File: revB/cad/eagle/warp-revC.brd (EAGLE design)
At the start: 38.1 x 38.1 mm, 145 parts, among them J2 QIIC connector, J3 QIIC connector, J4 DF40FC-20DP-0.4V(51)

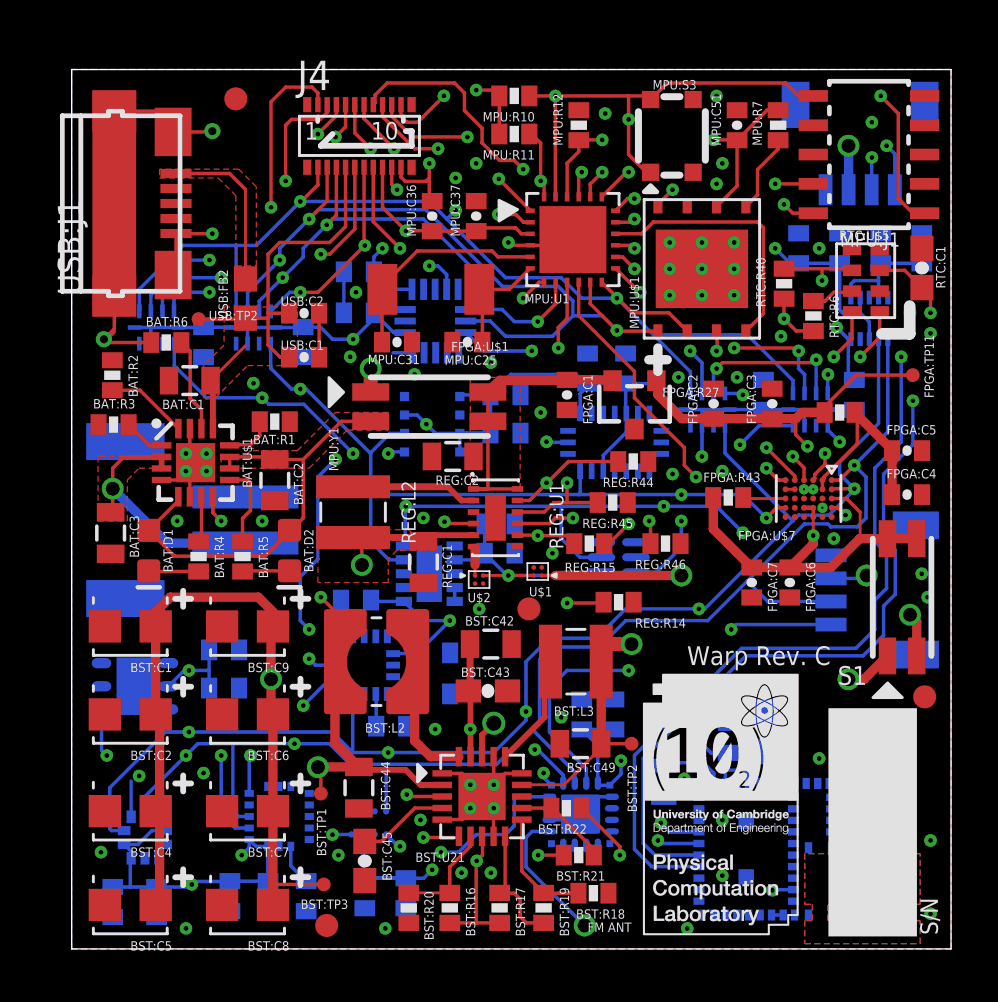
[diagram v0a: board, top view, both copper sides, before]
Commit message: Corrected DRC errors with layout and completed silkscreen
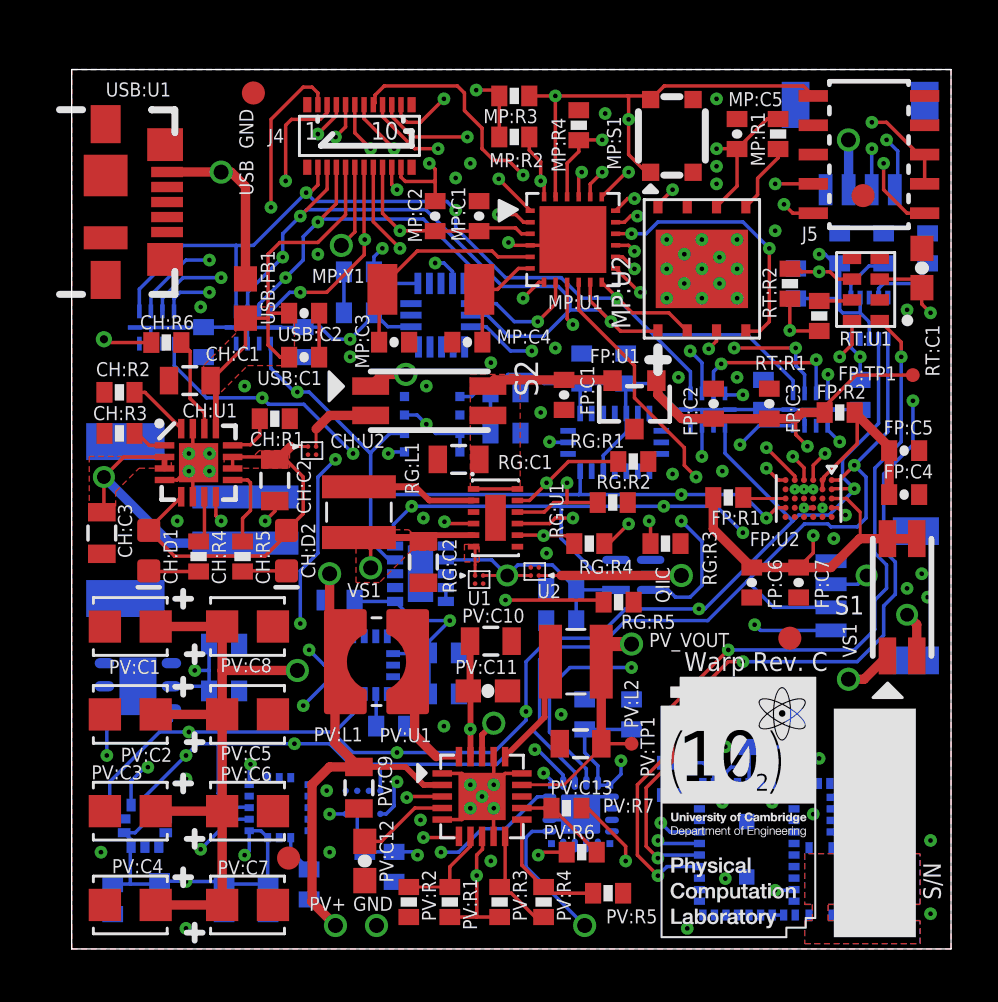
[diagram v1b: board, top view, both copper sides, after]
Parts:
- removed BAT:C3, BST:C42: 4.7uF, SparkFun-Passives:0805
- removed BAT:D2: (no value), SparkFun-LED:LED-0603
- removed BAT:R1: 2.94k, SparkFun-Passives:0402-RES
- removed BAT:R2: 4.32k, SparkFun-Passives:0402-RES
- removed BAT:R3, MPU:R11, MPU:R7, RTC:R40, RTC:R6: 10k, SparkFun-Passives:0402-RES
- removed BAT:U$1: BQ24230VQFN, BQ24230:PVQFN-N16
- removed BST:R16: 4.02M, SparkFun-Passives:0402-RES
- removed BST:R17: 1.3M, SparkFun-Passives:0402-RES
- removed BST:R18: 6.49M, SparkFun-Passives:0402-RES
- removed BST:R19: 5.36M, SparkFun-Passives:0402-RES
- removed BST:R20: 9.09M, SparkFun-Passives:0402-RES
- removed BST:R21: 8.87M, SparkFun-Passives:0402-RES
- removed BST:TP1, BST:TP3, USB:TP2: TPSTP06R, testpad:TP06R
- removed BT:C32, DP:C52, FPGA:C3, FPGA:C4, FPGA:C6, MPU:C37, MPU:C51, SEN1:C28, SEN2:C16, SEN2:C18, SEN2:C20, SEN2:C21, SEN2:C23, SEN2:C34, SEN2:C46, SEN2:C48: 0.1uF, SparkFun-Passives:0402-CAP
- removed DP:U20: ISL23415UTQFN, ISL23415:ISL23415
- removed FD5: FIDUCIAL1X2, SparkFun-Aesthetics:FIDUCIAL-1X2
- removed FPGA:C1, SEN1:C13, SEN1:C27, SEN1:C29, SEN2:C17, SEN2:C22, SEN2:C39, SEN2:C47: 1uF, SparkFun-Passives:0402-CAP
- removed FPGA:C5, SEN2:C15: 10uF, SparkFun-Passives:0402-CAP
- removed MPU:C31: 33pF, SparkFun-Passives:0402-CAP
- removed MPU:C36: 4.7uF (pol), SparkFun-Passives:0402-CAP
- removed REG:C2: 10uF, SparkFun-Passives:0805
- removed REG:L2: 2.2uH, EMCComponents (rev19c):WE-TPC_2828_OLD
- removed RTC:U$5: RV-8803-C7_RTC, Micro Crystal RTC:RV-C7
- removed S3: CHS-02_SWITCH, CHS_SWITCH:CHS-02_SWITCH
- removed SEN1:C50, SEN2:C19: 4.7uF, SparkFun-Passives:0402-CAP
- removed SEN1:U1: ADXL362, ADXL362:ADXL362
- removed SEN1:U10: TCS34725FN, TCS3772:TCS3772
- removed SEN1:U5: CCS811, SparkFun-Sensors:LGA10
- removed SEN2:C24: 10nF (25V), SparkFun-Passives:0402-CAP
- removed SEN2:C35: 22nF, SparkFun-Passives:0402-CAP
- removed SEN2:U16: LPS25H, LPS25H:LPS25H
- removed SEN2:U4: HDC1000, HDC1000:HDC1000
- removed SEN2:U5: L3GD20H, L3GD20H:L3GD20H
- removed SEN2:U9: SI7021, SI7021:SI7021
- removed U$1: MAX40200, MAX40200:DSBGA
- removed USB:J1: J_USB_MICROAB_HIROSE_ZX62-AB-5PA, j_usb_hirose_zx62-ab-5pa:J_USB_MICROAB_HIROSE_ZX62-AB-5PA
- added BT:C2, FP:C1, SA:C4, SA:C7, SA:C9, SB:C10, SB:C18, SB:C2, SB:C8: 1uF, SparkFun-Passives:0402-CAP
- added CH:C3, PV:C10: 4.7uF, SparkFun-Passives:0805
- added CH:D2: (no value), SparkFun-LED:LED-0603
- added CH:R1: 2.94k, SparkFun-Passives:0402-RES
- added CH:R2: 4.32k, SparkFun-Passives:0402-RES
- added CH:R3, MP:R1, MP:R2, RT:R1, RT:R2: 10k, SparkFun-Passives:0402-RES
- added CH:U1: BQ24230VQFN, BQ24230:PVQFN-N16
- added CH:U2, U2: MAX40200, MAX40200:DSBGA
- added DP:C4, FP:C3, FP:C4, FP:C7, MP:C1, MP:C5, SA:C8, SB:C1, SB:C11, SB:C12, SB:C13, SB:C16, SB:C17, SB:C4, SB:C7: 0.1uF, SparkFun-Passives:0402-CAP
- added DP:U4: ISL23415UTQFN, ISL23415:ISL23415
- added FD4: FIDUCIAL1X2, SparkFun-Aesthetics:FIDUCIAL-1X2
- added FP:C5, SB:C5: 10uF, SparkFun-Passives:0402-CAP
- added MP:C2: 4.7uF (pol), SparkFun-Passives:0402-CAP
- added MP:C3: 33pF, SparkFun-Passives:0402-CAP
- added PV:R1: 4.02M, SparkFun-Passives:0402-RES
- added PV:R2: 9.09M, SparkFun-Passives:0402-RES
- added PV:R3: 1.3M, SparkFun-Passives:0402-RES
- added PV:R4: 5.36M, SparkFun-Passives:0402-RES
- added PV:R5: 6.49M, SparkFun-Passives:0402-RES
- added PV:R6: 8.87M, SparkFun-Passives:0402-RES
- added RG:C1: 10uF, SparkFun-Passives:0805
- added RG:L1: 2.2uH, EMCComponents (rev19c):WE-TPC_2828_OLD
- added RT:U1: RV-8803-C7_RTC, Micro Crystal RTC:RV-C7
- added S2: CHS-02_SWITCH, CHS_SWITCH:CHS-02_SWITCH
- added SA:C5, SB:C14: 4.7uF, SparkFun-Passives:0402-CAP
- added SA:U1: ADXL362, ADXL362:ADXL362
- added SA:U3: CCS811, SparkFun-Sensors:LGA10
- added SA:U5: TCS34725FN, TCS3772:TCS3772
- added SB:C15: 22nF, SparkFun-Passives:0402-CAP
- added SB:C6: 10nF (25V), SparkFun-Passives:0402-CAP
- added SB:U2: L3GD20H, L3GD20H:L3GD20H
- added SB:U3: SI7021, SI7021:SI7021
- added SB:U5: LPS25H, LPS25H:LPS25H
- added SB:U7: HDC1000, HDC1000:HDC1000
- added USB:U1: MOLEX_USB_47346-0001MICRO_USB_B, MOLEX MICRO USB:USB-B-MICRO-SMD
- BT:C1: value 1uF -> 0.1uF; device SparkFun-Passives:0603-CAP -> SparkFun-Passives:0402-CAP
- BT:U1: value BGX13S -> BGX13S22GA-V21R
- MP:U2: value AT45DB641E -> AT45DB641E-MHN-Y
- moved FD1 33.0 mm to (9.40, 3.94)
- moved DP:C1 24.4 mm to (5.71, 26.3), turned to 270 degrees
- moved DP:U1 24.1 mm to (3.68, 26.9)
- moved FD2 23.0 mm to (34.3, 32.6)
- moved J2 17.6 mm to (32.9, 15.3), turned to 270 degrees
- moved J3 17.4 mm to (34.2, 32.9), turned to 180 degrees
- moved FD3 6.37 mm to (31.1, 13.5)
- moved DP:U2 4.44 mm to (27.6, 23.4)
- moved DP:C2 3.94 mm to (30.0, 24.0)
- moved BT:C1 0.76 mm to (29.3, 9.40)
- moved BT:Y1 0.28 mm to (25.9, 7.37)
- turned PV:C5 to 0 degrees
- turned PV:C6 to 0 degrees
- turned PV:C7 to 0 degrees
- turned PV:C8 to 0 degrees
- renumbered BAT:C1 to CH:C1, BAT:C2 to CH:C2, BAT:D1 to CH:D1, BAT:R4 to CH:R4, BAT:R5 to CH:R5, BAT:R6 to CH:R6, BST:C1 to PV:C1, BST:C2 to PV:C2, BST:C4 to PV:C3, BST:C43 to PV:C11, BST:C44 to PV:C9, BST:C45 to PV:C12, BST:C49 to PV:C13, BST:C5 to PV:C4, BST:C6 to PV:C5, BST:C7 to PV:C6, BST:C8 to PV:C7, BST:C9 to PV:C8, BST:L2 to PV:L1, BST:L3 to PV:L2, BST:R22 to PV:R7, BST:TP2 to PV:TP1, BST:U21 to PV:U1, DP:C53 to DP:C3, DP:U23 to DP:U3, FPGA:C2 to FP:C2, FPGA:C7 to FP:C6, FPGA:R27 to FP:R2, FPGA:R43 to FP:R1, FPGA:TP11 to FP:TP1, FPGA:U$1 to FP:U1, FPGA:U$7 to FP:U2, MPU:C25 to MP:C4, MPU:J1 to J5, MPU:R10 to MP:R3, MPU:R12 to MP:R4, MPU:S3 to MP:S1, MPU:U$1 to MP:U2, MPU:U1 to MP:U1, MPU:Y1 to MP:Y1, REG:C1 to RG:C2, REG:R14 to RG:R5, REG:R15 to RG:R4, REG:R44 to RG:R1, REG:R45 to RG:R2, REG:R46 to RG:R3, REG:U1 to RG:U1, RTC:C1 to RT:C1, SEN1:C10 to SA:C1, SEN1:C11 to SA:C2, SEN1:C12 to SA:C3, SEN1:C26 to SA:C6, SEN1:U2 to SA:U4, SEN1:U3 to SA:U2, SEN2:C14 to SB:C3, SEN2:C38 to SB:C9, SEN2:U13 to SB:U6, SEN2:U7 to SB:U4, SEN2:U8 to SB:U1, U$2 to U1, USB:FB2 to USB:FB1
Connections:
- net BAT:N$6 renamed CH:N$6
- net BST:LBOOST renamed PV:LBOOST
- net BST:LBUCK renamed PV:LBUCK
- net BST:VREF_SAMP renamed PV:VREF_SAMP
- net FPGA:CRESET_B renamed FP:CRESET_B
- net MPU:AT45DB321F_SPI_CS renamed MP:AT45DB321F_SPI_CS
- net MPU:XTAL0 renamed MP:XTAL0
- net SEN2:N$1 renamed SB:N$1
- net SEN2:SI4705_FMI renamed SB:SI4705_FMI
- removed net BAT:N$1: BAT:R2.2, BAT:U$1.16
- removed net BAT:N$2: BAT:R1.2, BAT:U$1.12
- removed net BAT:N$3: BAT:U$1.7, CH:R4.1
- removed net BAT:N$4: BAT:R3.2, BAT:U$1.1
- removed net BAT:N$5: BAT:U$1.9, CH:R5.1
- removed net BAT:N$7: BAT:D2.C, CH:R5.2
- removed net BAT:N$8: BAT:U$1.14, CH:R6.2
- removed net BOOST_VOUT: PV:C13.1, PV:L2.2, PV:TP1.TP, PV:U1.14, S3.1
- removed net BST:OK_HYST: BST:R17.1, BST:R19.2, PV:U1.10
- removed net BST:OK_PROG: BST:R18.2, BST:R19.1, PV:U1.11
- removed net BST:VBAT_OV: BST:R16.1, BST:R20.2, PV:U1.7
- removed net BST:VOUT_SET: BST:R21.1, PV:R7.2, PV:U1.12
- removed net BST:VRDIV: BST:R16.2, BST:R17.2, BST:R21.2, PV:U1.8
- removed net BST:VSTOR: BST:C42.1, PV:C11.1, PV:U1.19, PV:U1.3, PV:U1.6
- removed net FPGA:ICE40_VCC_PLL: FP:R2.1, FP:U2.B1, FP:U2.B2, FPGA:C4.1, FPGA:C5.1
- removed net FPGA:VCC_1V2: FP:C2.1, FP:R2.2, FP:TP1.TP, FP:U1.1, FP:U2.C2, FPGA:C3.1
- removed net MPU:EXTAL0: MP:U1.P$5, MP:Y1.P$1, MPU:C31.1
- removed net MPU:N$4: MP:U2.5, MPU:R7.1
- removed net PV_VS: BST:TP1.TP, J4.P$15, PV:C9.1, PV:L1.1, PV:U1.2
- removed net REG:SW: REG:L2.1, RG:U1.2
- removed net RTC:N$3: RTC:R6.1, RTC:U$5.7
- removed net SEN1:N$7: SEN1:U5.4, SEN1:U5.5
- removed net SEN2:CAP: SEN2:C24.1, SEN2:U5.P$14
- removed net SEN2:N$17: SB:U4.P$1, SB:U4.P$4, SEN2:C20.1, SEN2:C21.1
- removed net USB:DM: USB:J1.P$2
- removed net USB:DP: USB:J1.P$3
- new net CH:BQ24230_OUT: CH:C2.1, CH:D1.A, CH:D2.A, CH:U1.10, CH:U1.11, CH:U1.5, CH:U2.A1
- new net CH:N$1: CH:R2.2, CH:U1.16
- new net CH:N$2: CH:R1.2, CH:U1.12
- new net CH:N$3: CH:R4.1, CH:U1.7
- new net CH:N$4: CH:R3.2, CH:U1.1
- new net CH:N$5: CH:R5.1, CH:U1.9
- new net CH:N$7: CH:D2.C, CH:R5.2
- new net CH:N$8: CH:R6.2, CH:U1.14
- new net FP:ICE40_VCC_PLL: FP:C4.1, FP:C5.1, FP:R2.1, FP:U2.B1, FP:U2.B2
- new net FP:VCC_1V2: FP:C2.1, FP:C3.1, FP:R2.2, FP:TP1.TP, FP:U1.1, FP:U2.C2
- new net MP:EXTAL0: MP:C3.1, MP:U1.P$5, MP:Y1.P$1
- new net MP:N$4: MP:R1.1, MP:U2.5
- new net PV:OK_HYST: PV:R3.1, PV:R4.2, PV:U1.10
- new net PV:OK_PROG: PV:R4.1, PV:R5.2, PV:U1.11
- new net PV:VBAT_OV: PV:R1.1, PV:R2.2, PV:U1.7
- new net PV:VOUT_SET: PV:R6.1, PV:R7.2, PV:U1.12
- new net PV:VRDIV: PV:R1.2, PV:R3.2, PV:R6.2, PV:U1.8
- new net PV:VSTOR: PV:C10.1, PV:C11.1, PV:U1.19, PV:U1.3, PV:U1.6
- new net PV_VIN: J4.P$15, PV:C9.1, PV:L1.1, PV:U1.2
- new net PV_VOUT: PV:C13.1, PV:L2.2, PV:TP1.TP, PV:U1.14, S2.1
- new net RG:SW: RG:L1.1, RG:U1.2
- new net RT:N$3: RT:R1.1, RT:U1.7
- new net SA:N$7: SA:U3.4, SA:U3.5
- new net SB:CAP: SB:C6.1, SB:U2.P$14
- new net SB:N$17: SB:C12.1, SB:U4.P$1
- new net SB:N$2: SB:C11.1, SB:U4.P$4
- net ADXL362_SPI_CS: now also SA:U1.P$8; no longer SEN1:U1.P$8
- net BAT: now also CH:C3.1, CH:U1.2, CH:U1.3; no longer BAT:C3.1, BAT:U$1.2, BAT:U$1.3
- net BOOST_VBAT: no longer BST:TP3.TP
- net CHARGE_VOUT: now also CH:U2.A2, S2.2; no longer BAT:D2.A, BAT:U$1.10, BAT:U$1.11, BAT:U$1.5, CH:C2.1, CH:D1.A, S3.2
- net FPGA_VS: now also FP:C7.1; no longer FP:U2.C5, FPGA:C6.1
- net GND: now also BT:C2.2, CH:C3.2, CH:R1.1, CH:R2.1, CH:R3.1, CH:U1.15, CH:U1.4, CH:U1.6, CH:U1.8, CH:U1.EP, CH:U2.B2, DP:C4.2, DP:U4.9, FP:C1.2, FP:C3.2, FP:C4.2, FP:C5.2, FP:C7.2, MP:C1.2, MP:C2.2, MP:C3.2, MP:C5.2, PV:C10.2, PV:R2.1, PV:R5.1, RG:C1.2, RT:U1.4, RT:U1.5, SA:C4.2, SA:C5.2, SA:C7.2, SA:C8.2, SA:C9.2, SA:U1.P$12, SA:U1.P$13, SA:U1.P$16, SA:U3.1, SA:U3.7, SA:U3.EP, SA:U5.P$3, SB:C1.2, SB:C10.2, SB:C11.2, SB:C12.2, SB:C13.2, SB:C14.2, SB:C15.2, SB:C16.2, SB:C17.2, SB:C18.2, SB:C2.2, SB:C4.2, SB:C5.2, SB:C6.2, SB:C7.2, SB:C8.2, SB:U2.P$10, SB:U2.P$11, SB:U2.P$12, SB:U2.P$13, SB:U2.P$15, SB:U2.P$4, SB:U2.P$9, SB:U3.P$2, SB:U5.P$3, SB:U5.P$5, SB:U5.P$8, SB:U5.P$9, SB:U7.B2, U2.B2, USB:U1.GND, USB:U1.S1, USB:U1.S2, USB:U1.S3, USB:U1.S4, USB:U1.S5, USB:U1.S6; no longer BAT:C3.2, BAT:R1.1, BAT:R2.1, BAT:R3.1, BAT:U$1.15, BAT:U$1.4, BAT:U$1.6, BAT:U$1.8, BAT:U$1.EP, BST:C42.2, BST:R18.1, BST:R20.1, BT:C32.2, DP:C52.2, DP:U20.9, FP:U2.F2, FPGA:C1.2, FPGA:C3.2, FPGA:C4.2, FPGA:C5.2, FPGA:C6.2, MPU:C31.2, MPU:C36.2, MPU:C37.2, MPU:C51.2, REG:C2.2, RTC:U$5.4, RTC:U$5.5, SEN1:C13.2, SEN1:C27.2, SEN1:C28.2, SEN1:C29.2, SEN1:C50.2, SEN1:U1.P$12, SEN1:U1.P$13, SEN1:U1.P$16, SEN1:U10.P$3, SEN1:U5.1, SEN1:U5.7, SEN1:U5.EP, SEN2:C15.2, SEN2:C16.2, SEN2:C17.2, SEN2:C18.2, SEN2:C19.2, SEN2:C20.2, SEN2:C21.2, SEN2:C22.2, SEN2:C23.2, SEN2:C24.2, SEN2:C34.2, SEN2:C35.2, SEN2:C39.2, SEN2:C46.2, SEN2:C47.2, SEN2:C48.2, SEN2:U16.P$3, SEN2:U16.P$5, SEN2:U16.P$8, SEN2:U16.P$9, SEN2:U4.B2, SEN2:U5.P$10, SEN2:U5.P$11, SEN2:U5.P$12, SEN2:U5.P$13, SEN2:U5.P$15, SEN2:U5.P$4, SEN2:U5.P$9, SEN2:U9.P$2, U$1.B2, USB:J1.P$5, USB:J1.SHIELD1, USB:J1.SHIELD2, USB:J1.SHIELD3, USB:J1.SHIELD4
- net I2C0_SCL/UART_TX: now also RT:U1.8; no longer RTC:U$5.8
- net I2C0_SDA/UART_RX: now also RT:U1.1; no longer RTC:U$5.1
- net I2C1_SCL: now also DP:U1.6, J3.4, SA:U3.10, SA:U5.P$2; no longer DP:U20.6, J2.4, SEN1:U10.P$2, SEN1:U5.10
- net I2C1_SDA: now also J3.3, SA:U3.9, SA:U5.P$6; no longer J2.3, SEN1:U10.P$6, SEN1:U5.9
- net I2C2_SCL: now also DP:U2.6, J2.4, SB:U2.P$2, SB:U3.P$6, SB:U5.P$2, SB:U7.A1; no longer DP:U1.6, J3.4, SEN2:U16.P$2, SEN2:U4.A1, SEN2:U5.P$2, SEN2:U9.P$6
- net I2C2_SDA: now also DP:U4.6, J2.3, SB:U2.P$3, SB:U3.P$1, SB:U5.P$4, SB:U7.A2; no longer DP:U2.6, J3.3, SEN2:U16.P$4, SEN2:U4.A2, SEN2:U5.P$3, SEN2:U9.P$1
- net ISL23415_SPI_CS: now also DP:U4.4; no longer DP:U20.4
- net REG_VIN: now also FP:C1.1, RG:C1.1, S2.1', S2.2'; no longer FPGA:C1.1, REG:C2.1, S3.1', S3.2'
- net RTC_!INT!/RESET_B: now also RT:R2.1, RT:U1.6; no longer RTC:R40.1, RTC:U$5.6
- net SPI_MISO/UART_RTS: now also DP:U4.2, SA:U1.P$7; no longer DP:U20.2, SEN1:U1.P$7
- net SPI_MOSI/UART_CTS: now also DP:U4.3, SA:U1.P$6; no longer DP:U20.3, SEN1:U1.P$6
- net SPI_SCK: now also DP:U4.1, SA:U1.P$4; no longer DP:U20.1, SEN1:U1.P$4
- net SWD_DIO: now also MP:R2.1; no longer MPU:R11.1
- net USB:VBUS: now also USB:U1.VBUS; no longer USB:J1.P$1
- net USB_5V: now also CH:U1.13; no longer BAT:U$1.13, USB:TP2.TP
- net VCC_QIIC: now also U2.A1; no longer U$1.A1
- net VS1: now also MP:C1.1, MP:C2.1, MP:C5.1, MP:R1.2, MP:R2.2, RG:L1.2, RT:R1.2, RT:R2.2, RT:U1.3; no longer MPU:C36.1, MPU:C37.1, MPU:C51.1, MPU:R11.2, MPU:R7.2, REG:L2.2, RTC:R40.2, RTC:R6.2, RTC:U$5.3
- net VS2: now also BT:C2.1, DP:C4.1, DP:U4.10, DP:U4.5, DP:U4.8, SA:C4.1, SA:C5.1, SA:C7.1, SA:C8.1, SA:C9.1, SA:U1.P$1, SA:U1.P$14, SA:U3.2, SA:U3.6, SA:U5.P$1, SB:C1.1, SB:C10.1, SB:C13.1, SB:C14.1, SB:C15.1, SB:C16.1, SB:C17.1, SB:C18.1, SB:C2.1, SB:C4.1, SB:C5.1, SB:C7.1, SB:C8.1, SB:U2.P$1, SB:U2.P$16, SB:U2.P$5, SB:U3.P$5, SB:U5.P$1, SB:U5.P$10, SB:U5.P$6, SB:U7.B1, SB:U7.C1, SB:U7.D1, U2.A2; no longer BT:C32.1, DP:C52.1, DP:U20.10, DP:U20.5, DP:U20.8, SEN1:C13.1, SEN1:C27.1, SEN1:C28.1, SEN1:C29.1, SEN1:C50.1, SEN1:U1.P$1, SEN1:U1.P$14, SEN1:U10.P$1, SEN1:U5.2, SEN1:U5.6, SEN2:C15.1, SEN2:C16.1, SEN2:C17.1, SEN2:C18.1, SEN2:C19.1, SEN2:C22.1, SEN2:C23.1, SEN2:C34.1, SEN2:C35.1, SEN2:C39.1, SEN2:C46.1, SEN2:C47.1, SEN2:C48.1, SEN2:U16.P$1, SEN2:U16.P$10, SEN2:U16.P$6, SEN2:U4.B1, SEN2:U4.C1, SEN2:U4.D1, SEN2:U5.P$1, SEN2:U5.P$16, SEN2:U5.P$5, SEN2:U9.P$5, U$1.A2
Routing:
- net PV_VIN: track 0.00 -> 40.4 mm, vias 0 -> 3
- net PV_VS: track 35.3 -> 0.00 mm, vias 3 -> 0
- net PV_VOUT: track 0.00 -> 29.9 mm, vias 0 -> 2
- net BOOST_VOUT: track 29.5 -> 0.00 mm, vias 2 -> 0
- net CH:BQ24230_OUT: track 0.00 -> 17.2 mm
- net FPGA:VCC_1V2: track 16.5 -> 0.00 mm, vias 2 -> 0
- net FP:VCC_1V2: track 0.00 -> 16.5 mm, vias 0 -> 2
- net CHARGE_VOUT: track 19.8 -> 3.37 mm
- net PV:VSTOR: track 0.00 -> 14.5 mm, vias 0 -> 3
- net BST:VSTOR: track 14.4 -> 0.00 mm, vias 3 -> 0
- net PV:VRDIV: track 0.00 -> 10.1 mm, vias 0 -> 2
- net BST:VRDIV: track 9.91 -> 0.00 mm, vias 2 -> 0
- net MP:EXTAL0: track 0.00 -> 9.63 mm
- net MPU:EXTAL0: track 9.58 -> 0.00 mm
- net BOOST_VBAT: track 46.6 -> 38.0 mm
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- added copper zone on layer 1, net REG_LOAD
- removed copper zone on layer 1, net USB:VBUS
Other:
- board text added: "GND"
- board text added: "PV+"
- board text added: "PV_VOUT"
- board text added: "QIIC"
- board text added: "USB"
- board text added: "VS1"
